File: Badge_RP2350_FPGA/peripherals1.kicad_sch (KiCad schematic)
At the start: 0 parts

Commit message: add new schematic and footprint element (subject for verification, and edit schematics a bit
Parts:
- added U5: (no value), symbol stScreens:st7789noblk
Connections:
- new net GND: U5. (CS)
- new net GPIO18: U5. (CS)
- new net GPIO19: U5. (CS)
- new net GPIO2: U5. (CS)
- new net GPIO3: U5. (CS)
- new net GPIO4: U5. (CS)
- new net VCC: U5. (CS)
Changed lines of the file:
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@@
 	(generator_version "10.0")
 	(paper "A4")
+	(wire
+		(pts
+			(xy 60.96 39.37) (xy 64.77 39.37)
+		)
+		(stroke
+			(width 0)
+			(type default)
+		)
+	)
+	(wire
+		(pts
+			(xy 60.96 26.67) (xy 64.77 26.67)
+		)
+		(stroke
+			(width 0)
+			(type default)
+		)
+	)
+	(wire
+		(pts
+			(xy 60.96 34.29) (xy 64.77 34.29)
+		)
+		(stroke
+			(width 0)
+			(type default)
+		)
+	)
+	(wire
+		(pts
+			(xy 60.96 29.21) (xy 64.77 29.21)
+		)
+		(stroke
+			(width 0)
+			(type default)
+		)
+	)
+	(wire
+		(pts
+			(xy 60.96 36.83) (xy 64.77 36.83)
+		)
+		(stroke
+			(width 0)
+			(type default)
+		)
+	)
+	(wire
+		(pts
+			(xy 60.96 41.91) (xy 64.77 41.91)
+		)
+		(stroke
+			(width 0)
+			(type default)
+		)
+	)
+	(wire
+		(pts
+			(xy 60.96 31.75) (xy 64.77 31.75)
+		)
+		(stroke
+			(width 0)
+			(type default)
+		)
+	)
+	(label "GPIO18"
+		(at 64.77 31.75 0)
+		(effects
+			(font
+				(size 1.27 1.27)
+			)
+			(justify left bottom)
+		)
+	)
+	(label "GND"
+		(at 64.77 26.67 0)
+		(effects
+			(font
+				(size 1.27 1.27)
+			)
+			(justify left bottom)
+		)
+	)
+	(label "GPIO19"
+		(at 64.77 34.29 0)
+		(effects
+			(font
+				(size 1.27 1.27)
+			)
+			(justify left bottom)
+		)
+	)
+	(label "GPIO3"
+		(at 64.77 39.37 0)
+		(effects
+			(font
+				(size 1.27 1.27)
+			)
+			(justify left bottom)
+		)
+	)
+	(label "GPIO2"
+		(at 64.77 41.91 0)
+		(effects
+			(font
+				(size 1.27 1.27)
+			)
+			(justify left bottom)
+		)
+	)
+	(label "GPIO4"
+		(at 64.77 36.83 0)
+		(effects
+			(font
+				(size 1.27 1.27)
+			)
+			(justify left bottom)
+		)
+	)
+	(label "VCC"
+		(at 64.77 29.21 0)
+		(effects
+			(font
+				(size 1.27 1.27)
+			)
+			(justify left bottom)
+		)
+	)
+	(symbol
+		(lib_id "stScreens:st7789noblk")
+		(at 44.45 21.59 0)
+		(unit 1)
+		(body_style 1)
+		(exclude_from_sim no)
+		(in_bom yes)
+		(on_board yes)
+		(in_pos_files yes)
+		(dnp no)
+		(fields_autoplaced yes)
+		(property "Reference" "U5"
+			(at 44.45 20.32 0)
+			(show_name no)
+			(do_not_autoplace no)
+			(effects
+				(font
+					(size 1.27 1.27)
+				)
+			)
+		)
+		(property "Value" ""
+			(at 44.45 21.59 0)
+			(show_name no)
+			(do_not_autoplace no)
+			(effects
+				(font
+					(size 1.27 1.27)
+				)
+			)
+		)
+		(property "Footprint" ""
+			(at 44.45 21.59 0)
+			(hide yes)
+			(show_name no)
+			(do_not_autoplace no)
+			(effects
+				(font
+					(size 1.27 1.27)
+				)
+			)
+		)
+		(property "Datasheet" ""
+			(at 44.45 21.59 0)
+			(hide yes)
+			(show_name no)
+			(do_not_autoplace no)
+			(effects
+				(font
+					(size 1.27 1.27)
+				)
+			)
+		)
+		(property "Description" ""
+			(at 44.45 21.59 0)
+			(hide yes)
+			(show_name no)
+			(do_not_autoplace no)
+			(effects
+				(font
+					(size 1.27 1.27)
+				)
+			)
+		)
+		(pin ""
+		)
+		(pin ""
+		)
+		(pin ""
+		)
+		(pin ""
+		)
+		(pin ""
+		)
+		(pin ""
+		)
+		(pin ""
+		)
+		(instances
+			(project "Badge_RP2350_FPGA"
+				(path "/0ce87b49-0553-4a87-87c1-84e31180901e/e2446d2b-ae35-4e61-9554-78e9a4abd0b0"
+					(reference "U5")
+					(unit 1)
+				)
+			)
+		)
+	)
 )

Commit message: edit custom st7789 footprint
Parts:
- U5: footprint (none) -> st7789screens:st7789_7pin_noblk
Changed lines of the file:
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@@
 			)
 		)
-		(property "Footprint" ""
+		(property "Footprint" "st7789screens:st7789_7pin_noblk"
 			(at 44.45 21.59 0)
 			(hide yes)

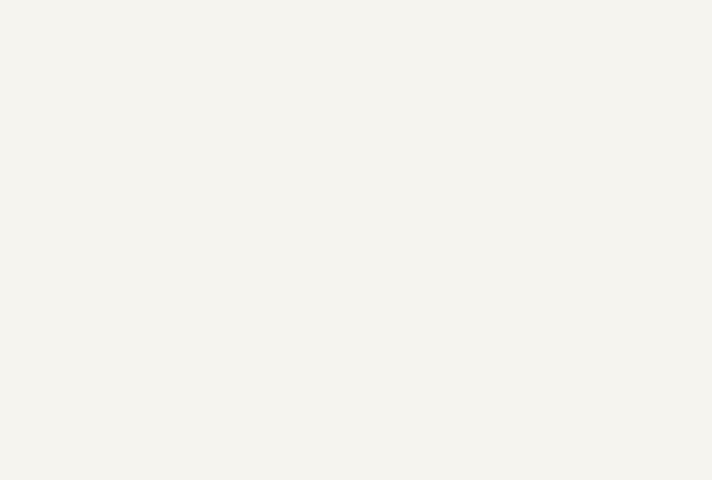
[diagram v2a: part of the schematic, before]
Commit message: add buttons by Arianna and make Flash 2 shared between 2 chips
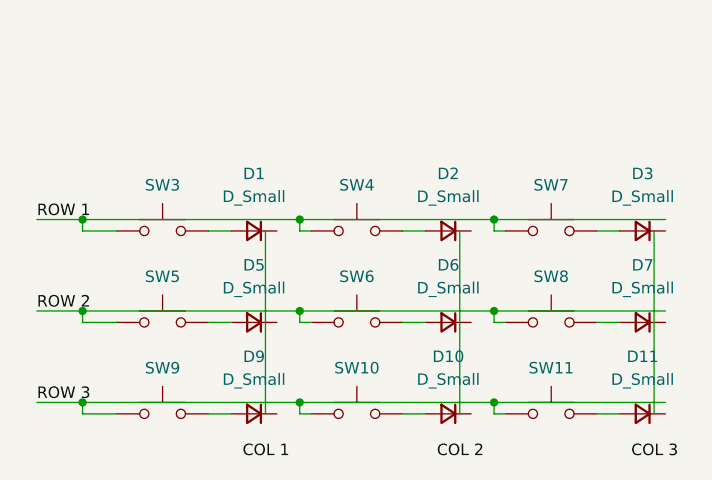
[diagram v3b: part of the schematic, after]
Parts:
- added D1, D10, D11, D2, D3, D5, D6, D7, D9: D_Small, symbol Device:D_Small
- added SW10, SW11, SW3, SW4, SW5, SW6, SW7, SW8, SW9: (no value), symbol Switch:SW_Push
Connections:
- new net: D5.2 (A), SW5.2
- new net: D3.2 (A), SW7.2
- new net: D9.2 (A), SW9.2
- new net: D6.2 (A), SW6.2
- new net: D7.2 (A), SW8.2
- new net: D1.2 (A), SW3.2
- new net: D10.2 (A), SW10.2
- new net: D2.2 (A), SW4.2
- new net: D11.2 (A), SW11.2
- new net ROW 1: SW3.1, SW4.1, SW7.1
- new net ROW 2: SW5.1, SW6.1, SW8.1
- new net ROW 3: SW10.1, SW11.1, SW9.1

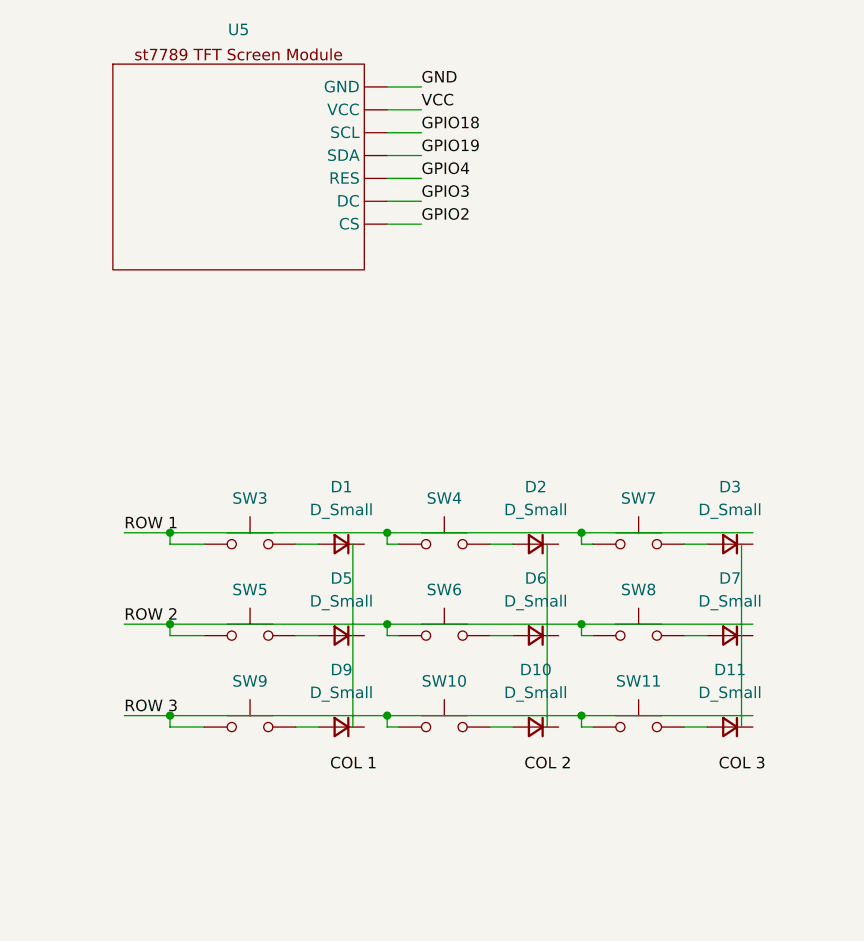
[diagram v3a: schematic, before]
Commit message: delete Core directory - not the right repository
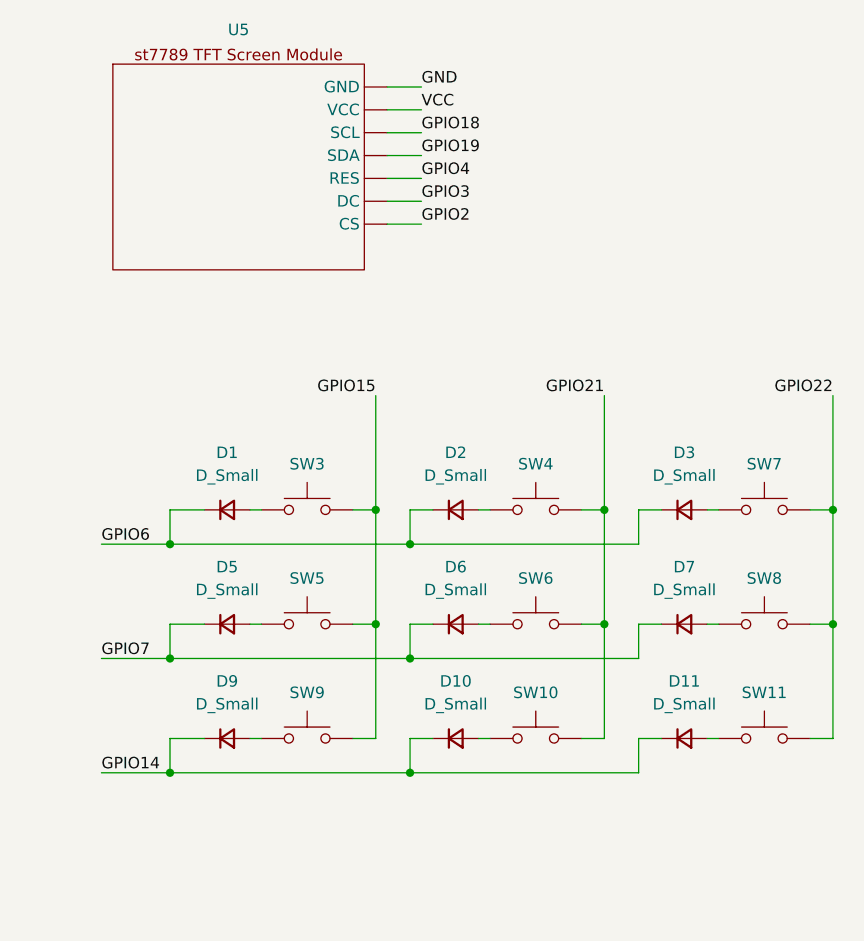
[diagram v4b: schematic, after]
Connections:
- net at D5.2 (A): now also SW5.1; no longer SW5.2
- net at D3.2 (A): now also SW7.1; no longer SW7.2
- net GPIO14: now reaches D9.1 (K)
- net GPIO14: now also D10.1 (K), D11.1 (K)
- net at D9.2 (A): now also SW9.1; no longer SW9.2
- net GPIO7: now reaches D6.1 (K)
- net GPIO7: now also D5.1 (K), D7.1 (K)
- net at D6.2 (A): now also SW6.1; no longer SW6.2
- net at D7.2 (A): now also SW8.1; no longer SW8.2
- net GPIO6: now reaches D1.1 (K)
- net GPIO6: now also D2.1 (K), D3.1 (K)
- net at D1.2 (A): now also SW3.1; no longer SW3.2
- net at D10.2 (A): now also SW10.1; no longer SW10.2
- net at D2.2 (A): now also SW4.1; no longer SW4.2
- net at D11.2 (A): now also SW11.1; no longer SW11.2
- removed net ROW 1: SW3.1, SW4.1, SW7.1
- removed net ROW 2: SW5.1, SW6.1, SW8.1
- removed net ROW 3: SW10.1, SW11.1, SW9.1
- new net GPIO15: SW3.2, SW5.2, SW9.2
- new net GPIO21: SW10.2, SW4.2, SW6.2
- new net GPIO22: SW11.2, SW7.2, SW8.2
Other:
- moved on the sheet: SW3, SW5, SW9

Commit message: add type c port and uart connections
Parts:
- D1, D10, D11, D2, D3, D5, D6, D7, D9: footprint (none) -> Diode_SMD:D_SOD-123
- SW10, SW11, SW3, SW4, SW5, SW6, SW7, SW8, SW9: footprint (none) -> Button_Switch_SMD:SW_Push_1P1T_NO_CK_KSC6xxG
- U5: footprint st7789screens:st7789_7pin_noblk -> semitovpartslibrary:st7789_7pin_noblk
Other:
- company: (none) -> SemiTO-V, RISC-V Student Team
- title: (none) -> RISC-V Summit Europe Badge
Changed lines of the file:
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@@
 	(generator_version "10.0")
 	(paper "A4")
+	(title_block
+		(title "RISC-V Summit Europe Badge")
+		(date "2026-03-29")
+		(rev "v1.0")
+		(company "SemiTO-V, RISC-V Student Team")
+		(comment 3 "License: CERN-OHL-W")
+		(comment 4 "Authors: Tan Siret Akıncı, Alessandro Bochino, Carlo Bendelli, Arianna Bruno")
+	)
 	(junction
 		(at 59.69 73.66)
@@
 			)
 		)
-		(property "Footprint" ""
+		(property "Footprint" "Button_Switch_SMD:SW_Push_1P1T_NO_CK_KSC6xxG"
 			(at 52.07 81.28 0)
 			(hide yes)
@@
 			)
 		)
-		(property "Footprint" ""
+		(property "Footprint" "Button_Switch_SMD:SW_Push_1P1T_NO_CK_KSC6xxG"
 			(at 102.87 68.58 0)
 			(hide yes)
@@
 			)
 		)
-		(property "Footprint" ""
+		(property "Footprint" "Diode_SMD:D_SOD-123"
 			(at 43.18 73.66 90)
 			(hide yes)
@@
 			)
 		)
-		(property "Footprint" ""
+		(property "Footprint" "Button_Switch_SMD:SW_Push_1P1T_NO_CK_KSC6xxG"
 			(at 52.07 93.98 0)
 			(hide yes)
@@
 			)
 		)
-		(property "Footprint" ""
+		(property "Footprint" "Diode_SMD:D_SOD-123"
 			(at 68.58 99.06 90)
 			(hide yes)
@@
 			)
 		)
-		(property "Footprint" ""
+		(property "Footprint" "Diode_SMD:D_SOD-123"
 			(at 93.98 86.36 90)
 			(hide yes)
@@
 			)
 		)
-		(property "Footprint" ""
+		(property "Footprint" "Button_Switch_SMD:SW_Push_1P1T_NO_CK_KSC6xxG"
 			(at 77.47 81.28 0)
 			(hide yes)
@@
 			)
 		)
-		(property "Footprint" ""
+		(property "Footprint" "Diode_SMD:D_SOD-123"
 			(at 43.18 99.06 90)
 			(hide yes)
@@
 			)
 		)
-		(property "Footprint" ""
+		(property "Footprint" "Diode_SMD:D_SOD-123"
 			(at 68.58 86.36 90)
 			(hide yes)
@@
 			)
 		)
-		(property "Footprint" ""
+		(property "Footprint" "Diode_SMD:D_SOD-123"
 			(at 93.98 73.66 90)
 			(hide yes)
@@
 			)
 		)
-		(property "Footprint" ""
+		(property "Footprint" "Button_Switch_SMD:SW_Push_1P1T_NO_CK_KSC6xxG"
 			(at 102.87 93.98 0)
 			(hide yes)
@@
 			)
 		)
-		(property "Footprint" ""
+		(property "Footprint" "Button_Switch_SMD:SW_Push_1P1T_NO_CK_KSC6xxG"
 			(at 102.87 81.28 0)
 			(hide yes)
@@
 			)
 		)
-		(property "Footprint" ""
+		(property "Footprint" "Button_Switch_SMD:SW_Push_1P1T_NO_CK_KSC6xxG"
 			(at 52.07 68.58 0)
 			(hide yes)
@@
 			)
 		)
-		(property "Footprint" ""
+		(property "Footprint" "Diode_SMD:D_SOD-123"
 			(at 43.18 86.36 90)
 			(hide yes)
@@
 			)
 		)
-		(property "Footprint" ""
+		(property "Footprint" "Button_Switch_SMD:SW_Push_1P1T_NO_CK_KSC6xxG"
 			(at 77.47 93.98 0)
 			(hide yes)
@@
 			)
 		)
-		(property "Footprint" ""
+		(property "Footprint" "Diode_SMD:D_SOD-123"
 			(at 68.58 73.66 90)
 			(hide yes)
@@
 			)
 		)
-		(property "Footprint" "st7789screens:st7789_7pin_noblk"
+		(property "Footprint" "semitovpartslibrary:st7789_7pin_noblk"
 			(at 44.45 21.59 0)
 			(hide yes)
@@
 			)
 		)
-		(property "Footprint" ""
+		(property "Footprint" "Diode_SMD:D_SOD-123"
 			(at 93.98 99.06 90)
 			(hide yes)
@@
 			)
 		)
-		(property "Footprint" ""
+		(property "Footprint" "Button_Switch_SMD:SW_Push_1P1T_NO_CK_KSC6xxG"
 			(at 77.47 68.58 0)
 			(hide yes)

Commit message: edit schematics, add global pins
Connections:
- net GPIO19 is gone; now on net SDA_TFT: U5. (CS)
- net GPIO2 is gone; now on net SDA_TFT: U5. (CS)
- net GPIO3 is gone; now on net SDA_TFT: U5. (CS)
- net GPIO4 is gone; now on net SDA_TFT: U5. (CS)
- net VCC is gone; now on net SDA_TFT: U5. (CS)
- net GPIO14 renamed ROW3
- net GPIO15 renamed COL1
- net GPIO18 renamed SDA_TFT
- net GPIO21 renamed COL2
- net GPIO22 renamed COL3
- net GPIO6 renamed ROW1
- net GPIO7 renamed ROW2
- new net + 3v3: U5. (CS)
- new net CS_TFT: U5. (CS)
- new net DC_TFT: U5. (CS)
- new net RES_TFT: U5. (CS)
- new net SCL_TFT: U5. (CS)
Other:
- note added: "Buttons matrix"
- note added: "TFT Screen"
- moved on the sheet: D1, D10, D11, D2, D3, D5, D6, D7, D9, SW10, SW11, SW3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

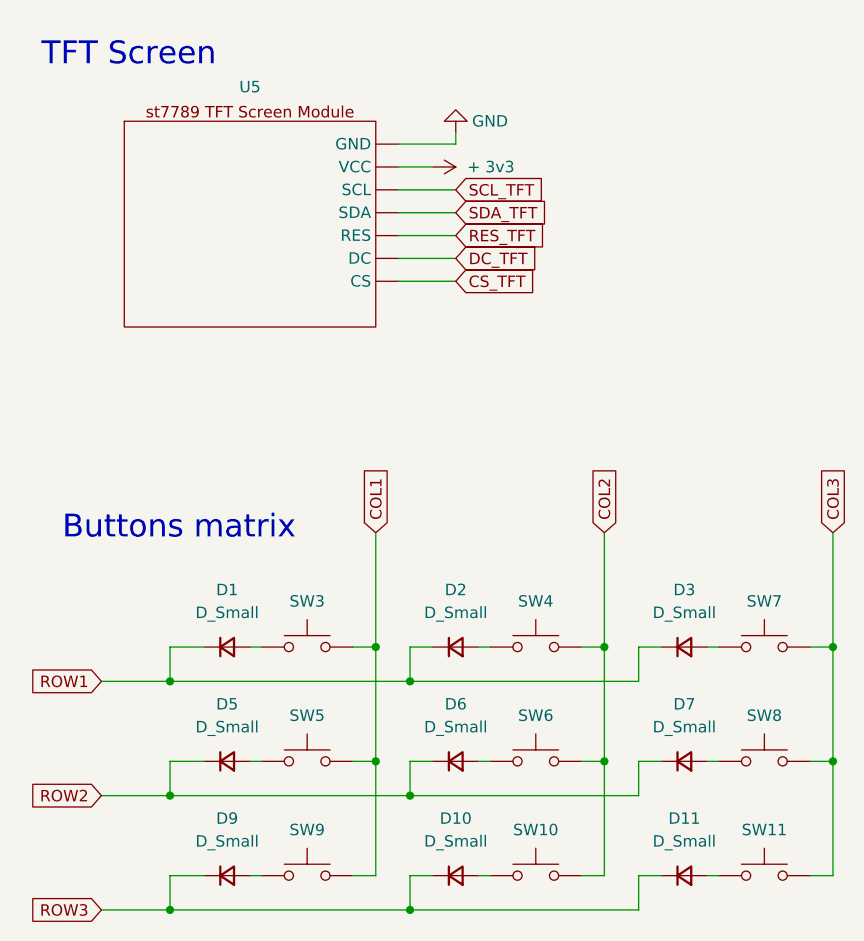
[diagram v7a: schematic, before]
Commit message: assign all footprints and import to pcb
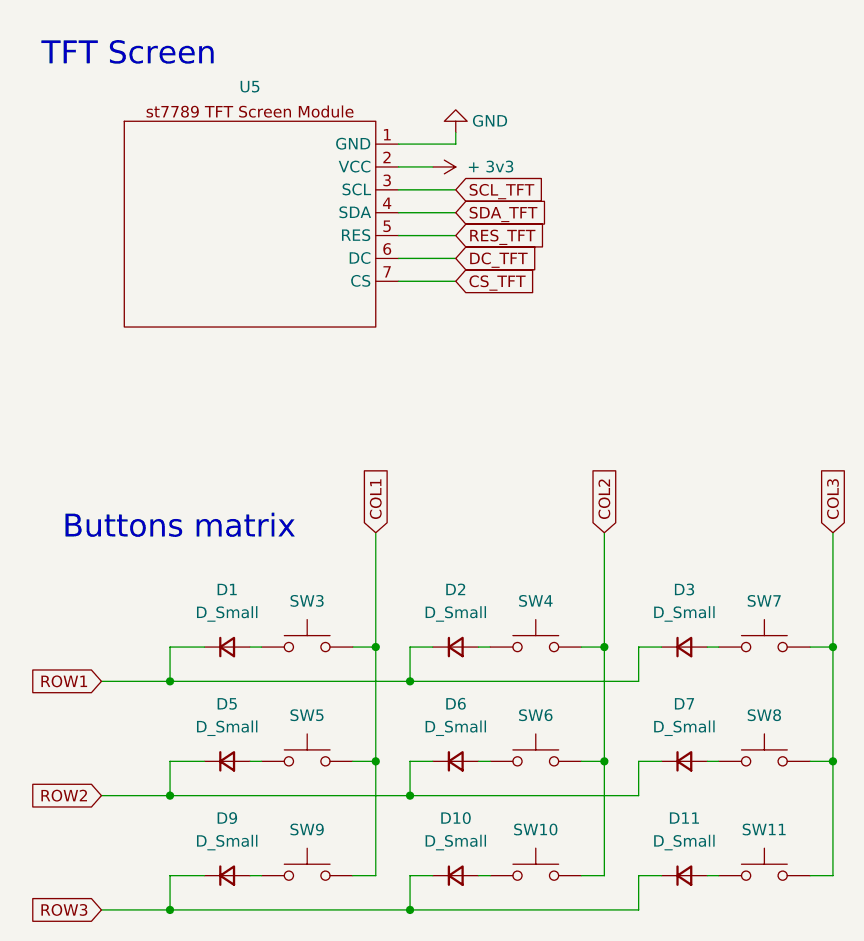
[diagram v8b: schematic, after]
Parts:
- SW10, SW11, SW3, SW4, SW5, SW6, SW7, SW8, SW9: footprint Button_Switch_SMD:SW_Push_1P1T_NO_CK_KSC6xxG -> Button_Switch_SMD:SW_SPST_PTS647_Sx38
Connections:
- net + 3v3: now also U5.2 (VCC); no longer U5. (CS)
- net CS_TFT: now also U5.7 (CS); no longer U5. (CS)
- net DC_TFT: now also U5.6 (DC); no longer U5. (CS)
- net GND: now also U5.1 (GND); no longer U5. (CS)
- net RES_TFT: now also U5.5 (RES); no longer U5. (CS)
- net SCL_TFT: now also U5.3 (SCL); no longer U5. (CS)
- net SDA_TFT: now also U5.4 (SDA); no longer U5. (CS)
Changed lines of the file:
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@@
 			)
 		)
-		(property "Footprint" "Button_Switch_SMD:SW_Push_1P1T_NO_CK_KSC6xxG"
+		(property "Footprint" "Button_Switch_SMD:SW_SPST_PTS647_Sx38"
 			(at 52.07 96.52 0)
 			(hide yes)
@@
 			)
 		)
-		(property "Footprint" "Button_Switch_SMD:SW_Push_1P1T_NO_CK_KSC6xxG"
+		(property "Footprint" "Button_Switch_SMD:SW_SPST_PTS647_Sx38"
 			(at 102.87 83.82 0)
 			(hide yes)
@@
 			)
 		)
-		(property "Footprint" "Button_Switch_SMD:SW_Push_1P1T_NO_CK_KSC6xxG"
+		(property "Footprint" "Button_Switch_SMD:SW_SPST_PTS647_Sx38"
 			(at 52.07 109.22 0)
 			(hide yes)
@@
 			)
 		)
-		(property "Footprint" "Button_Switch_SMD:SW_Push_1P1T_NO_CK_KSC6xxG"
+		(property "Footprint" "Button_Switch_SMD:SW_SPST_PTS647_Sx38"
 			(at 77.47 96.52 0)
 			(hide yes)
@@
 			)
 		)
-		(property "Footprint" "Button_Switch_SMD:SW_Push_1P1T_NO_CK_KSC6xxG"
+		(property "Footprint" "Button_Switch_SMD:SW_SPST_PTS647_Sx38"
 			(at 102.87 109.22 0)
 			(hide yes)
@@
 			)
 		)
-		(property "Footprint" "Button_Switch_SMD:SW_Push_1P1T_NO_CK_KSC6xxG"
+		(property "Footprint" "Button_Switch_SMD:SW_SPST_PTS647_Sx38"
 			(at 102.87 96.52 0)
 			(hide yes)
@@
 			)
 		)
-		(property "Footprint" "Button_Switch_SMD:SW_Push_1P1T_NO_CK_KSC6xxG"
+		(property "Footprint" "Button_Switch_SMD:SW_SPST_PTS647_Sx38"
 			(at 52.07 83.82 0)
 			(hide yes)
@@
 			)
 		)
-		(property "Footprint" "Button_Switch_SMD:SW_Push_1P1T_NO_CK_KSC6xxG"
+		(property "Footprint" "Button_Switch_SMD:SW_SPST_PTS647_Sx38"
 			(at 77.47 109.22 0)
 			(hide yes)
@@
 			)
 		)
-		(pin ""
-		)
-		(pin ""
-		)
-		(pin ""
-		)
-		(pin ""
-		)
-		(pin ""
-		)
-		(pin ""
-		)
-		(pin ""
+		(pin "3"
+		)
+		(pin "5"
+		)
+		(pin "2"
+		)
+		(pin "1"
+		)
+		(pin "6"
+		)
+		(pin "7"
+		)
+		(pin "4"
 		)
 		(instances
@@
 			)
 		)
-		(property "Footprint" "Button_Switch_SMD:SW_Push_1P1T_NO_CK_KSC6xxG"
+		(property "Footprint" "Button_Switch_SMD:SW_SPST_PTS647_Sx38"
 			(at 77.47 83.82 0)
 			(hide yes)
